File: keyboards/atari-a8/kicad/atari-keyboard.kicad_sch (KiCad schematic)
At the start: 24 parts, among them J101 PLAYER 1, J102 5V, J103 I2C DISPLAY, SW101 RESET, U101 Elite-C, U102 MAX7219, U103 MAX7219

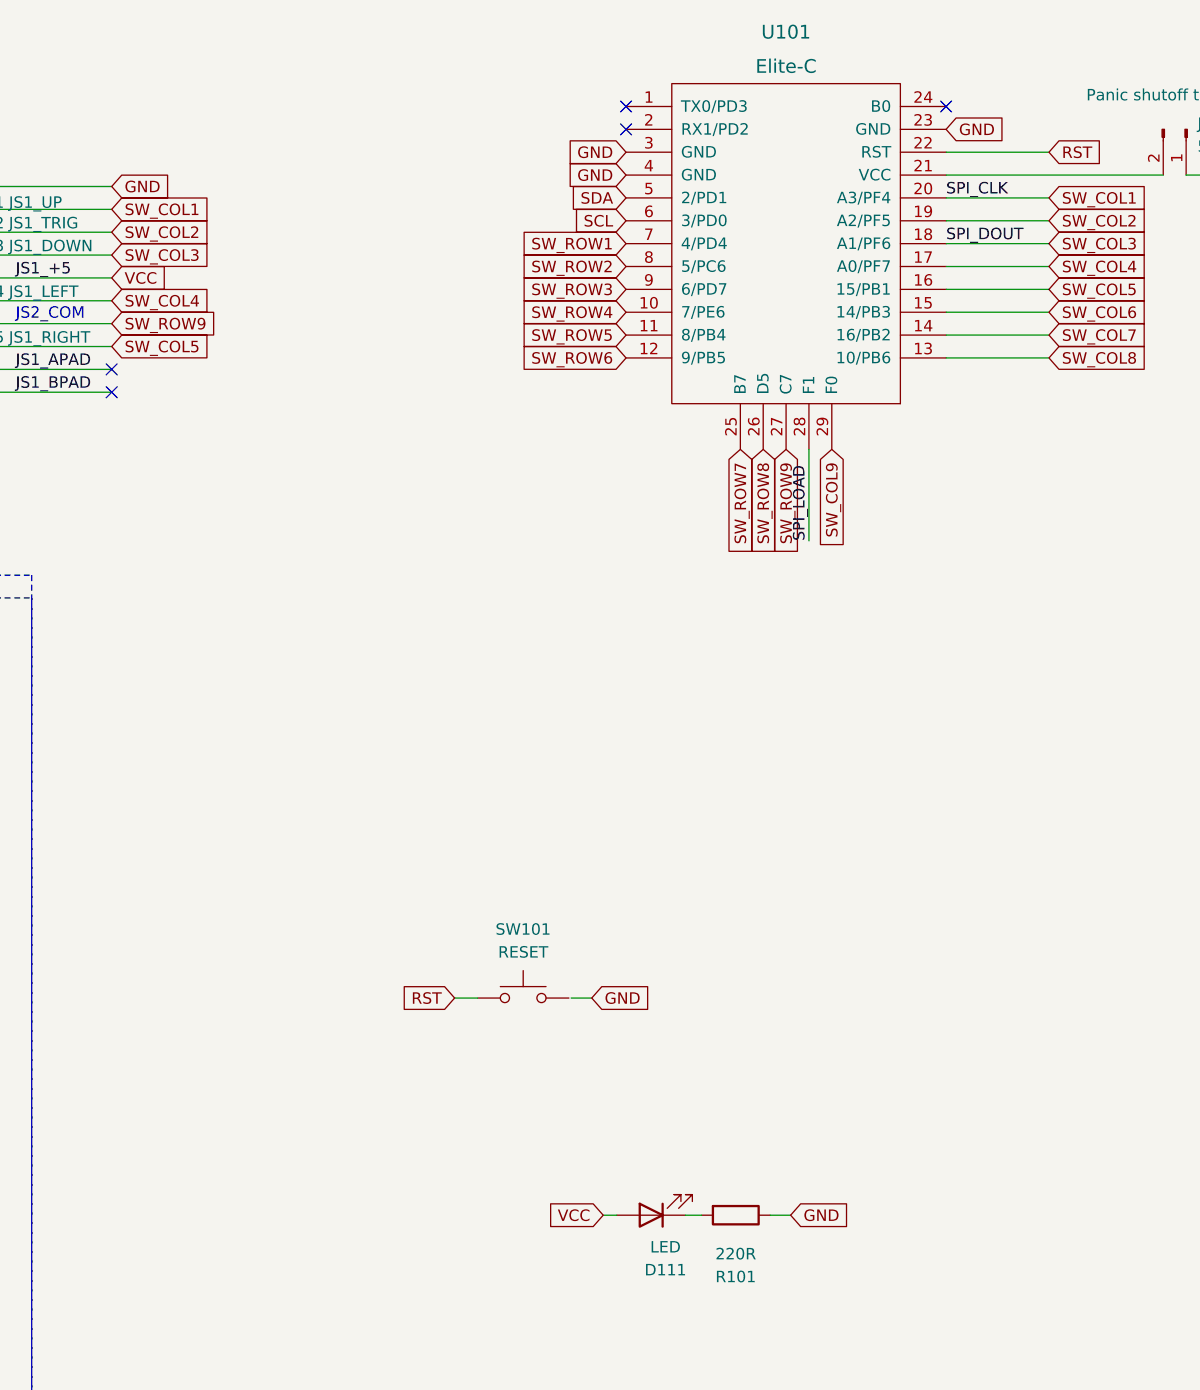
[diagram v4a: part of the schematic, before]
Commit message: Added the 16x2 LED option
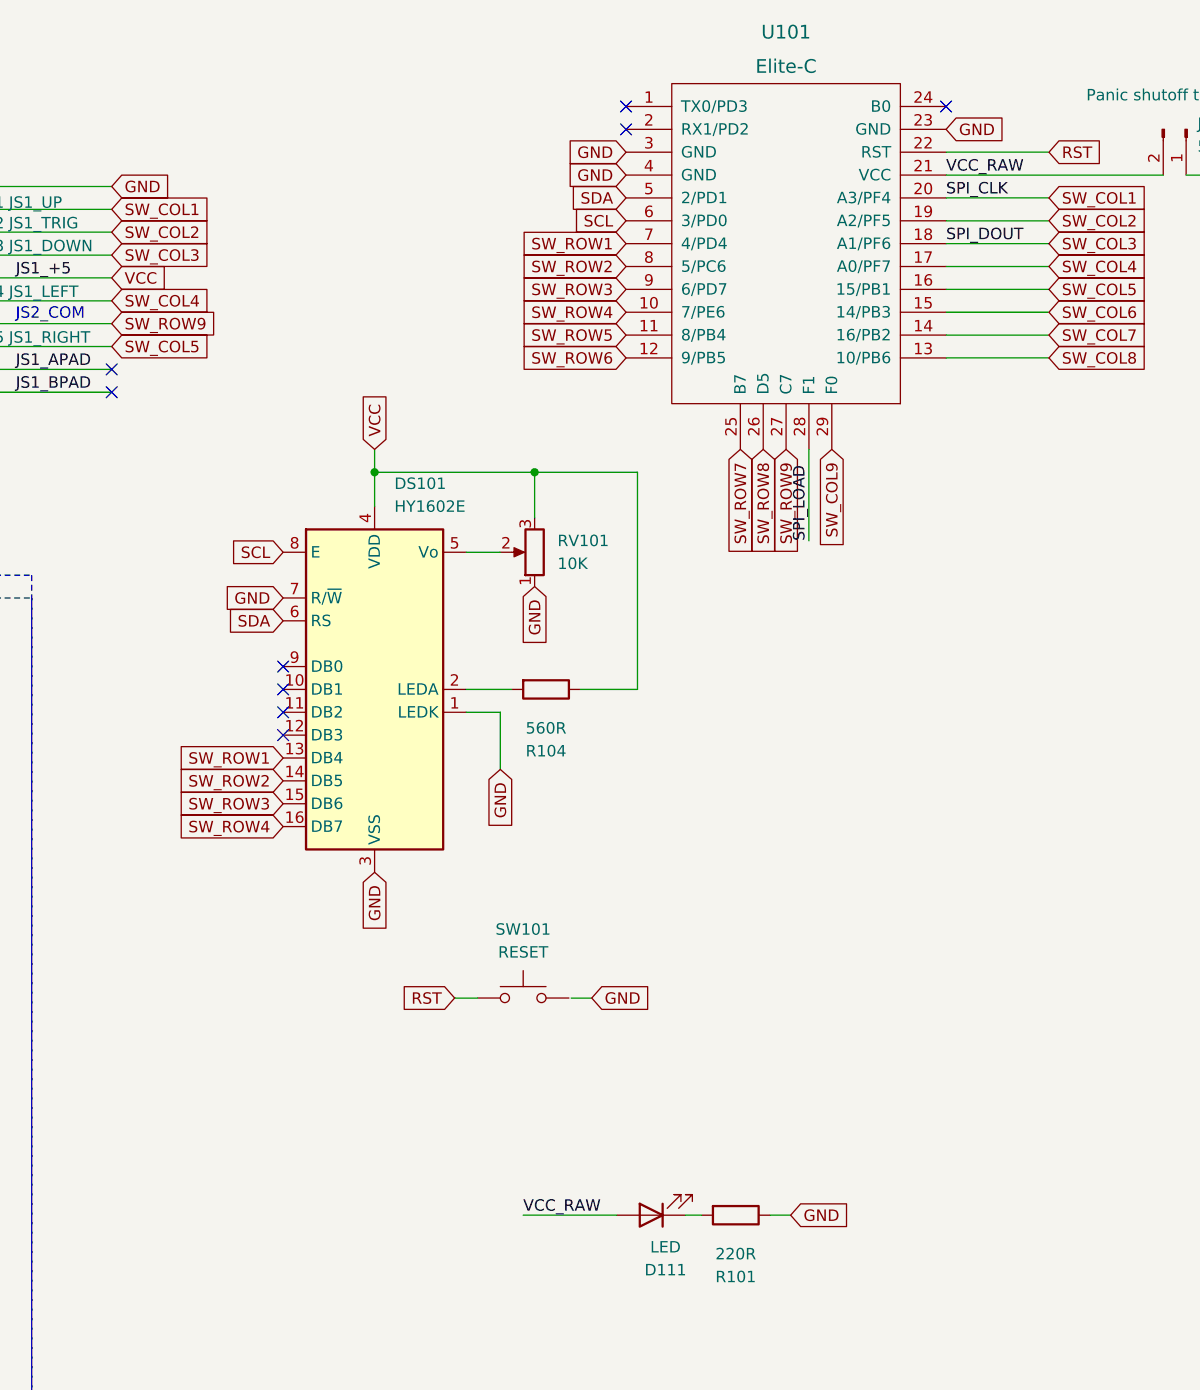
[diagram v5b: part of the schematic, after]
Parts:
- added DS101: HY1602E, Display:HY1602E, symbol Display_Character:HY1602E
- added R104: 560R, keebio:Resistor-Hybrid, symbol Device:R
- added RV101: 10K, Potentiometer_THT:Potentiometer_ACP_CA9-V10_Vertical, symbol Device:R_Potentiometer
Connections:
- net GND: now also DS101.1 (LEDK), DS101.3 (VSS), DS101.7 (R/~{W}), RV101.1
- net SCL: now also DS101.8 (E)
- net SDA: now also DS101.6 (RS)
- net SW_ROW1: now also DS101.13 (DB4)
- net SW_ROW2: now also DS101.14 (DB5)
- net SW_ROW3: now also DS101.15 (DB6)
- net SW_ROW4: now also DS101.16 (DB7)
- net VCC: now also DS101.4 (VDD), R104.1, RV101.3; no longer D111.2 (A)
- net VCC_RAW: now reaches J102.2 (Pin_2), U101.21 (VCC)
- net VCC_RAW: now also D111.2 (A)
- new net: DS101.2 (LEDA), R104.2
- new net: DS101.5 (Vo), RV101.2
- no-connect marks 5 -> 9

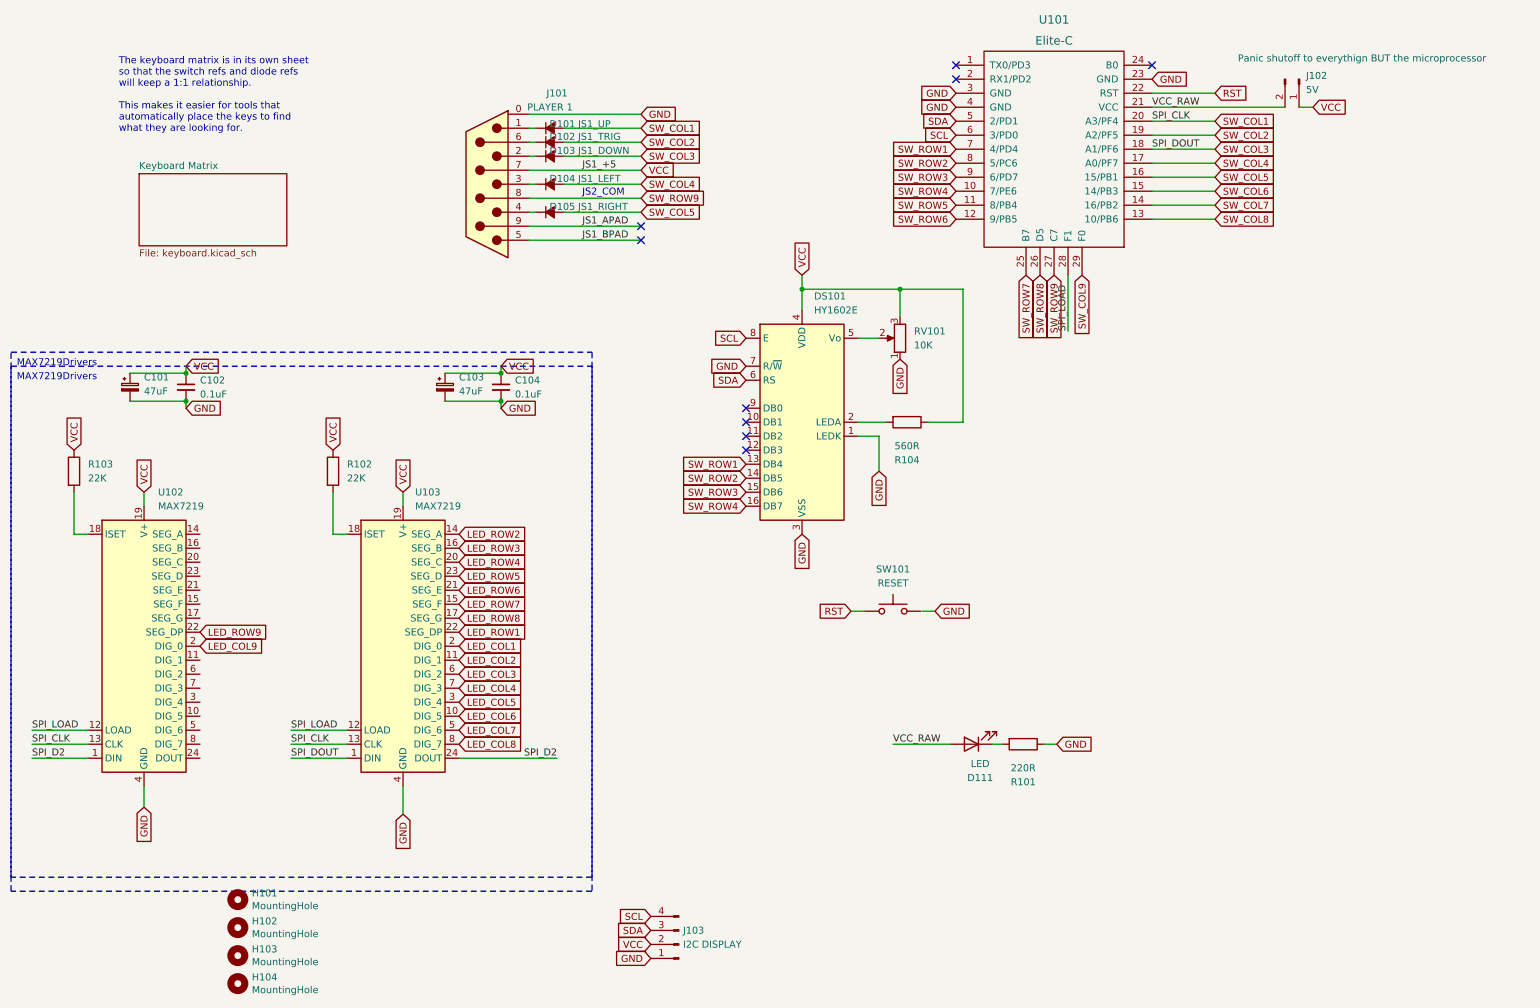
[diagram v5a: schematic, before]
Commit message: Re-arranged keys and layout for LCD screen
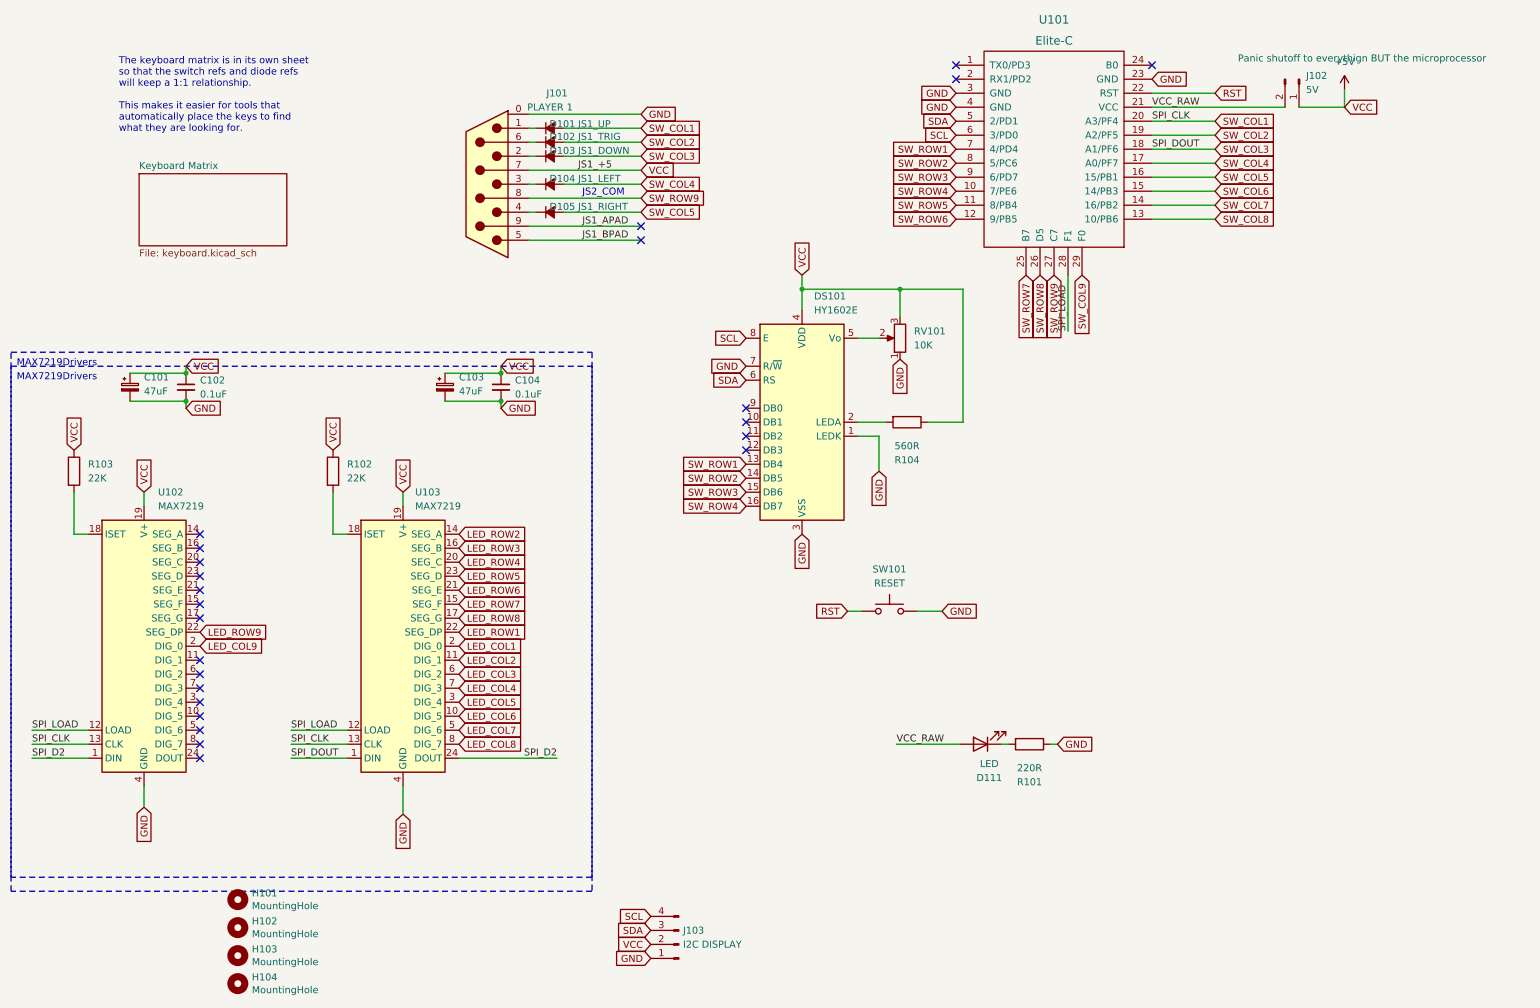
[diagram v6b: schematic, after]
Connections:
- net GND: now also SW101.2
- net VCC renamed +5V
- no-connect marks 9 -> 24
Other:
- moved on the sheet: D111, R101, SW101

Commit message: A bunch of changes to support the new layout
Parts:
- added C105, C106: 0.1uF, Capacitor_THT:C_Axial_L3.8mm_D2.6mm_P10.00mm_Horizontal, symbol Device:C_Small
- added U104: 7402, Package_DIP:DIP-14_W7.62mm_Socket_LongPads, symbol 74xx:7402
- added U105: 74LS08, Package_DIP:DIP-14_W7.62mm_Socket_LongPads, symbol 74xx:74LS08
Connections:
- net +5V: now also C105.1, C106.1, U104.14 (VCC), U105.14 (VCC)
- net GND: now also C105.2, C106.2, U104.7 (GND), U105.7 (GND)
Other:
- moved on the sheet: D111, R101
